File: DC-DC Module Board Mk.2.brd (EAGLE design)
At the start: 177.9 x 101.7 mm, 163 parts, among them Q1 FDN340P, U2 AP1117_LIN_REG, U3 LM1085IS-5.0

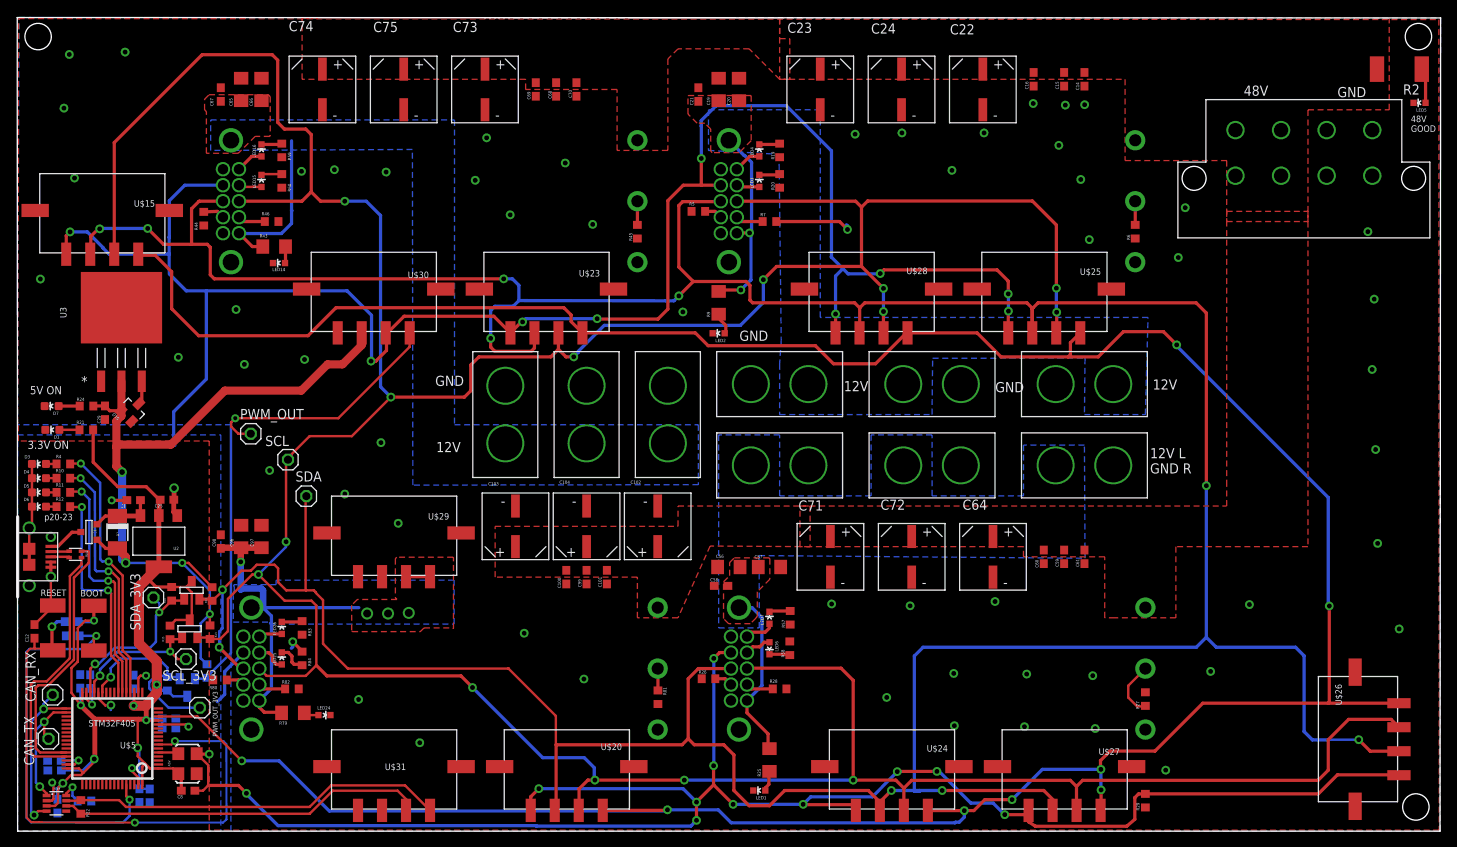
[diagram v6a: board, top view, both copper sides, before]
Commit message: cleaning up the trace
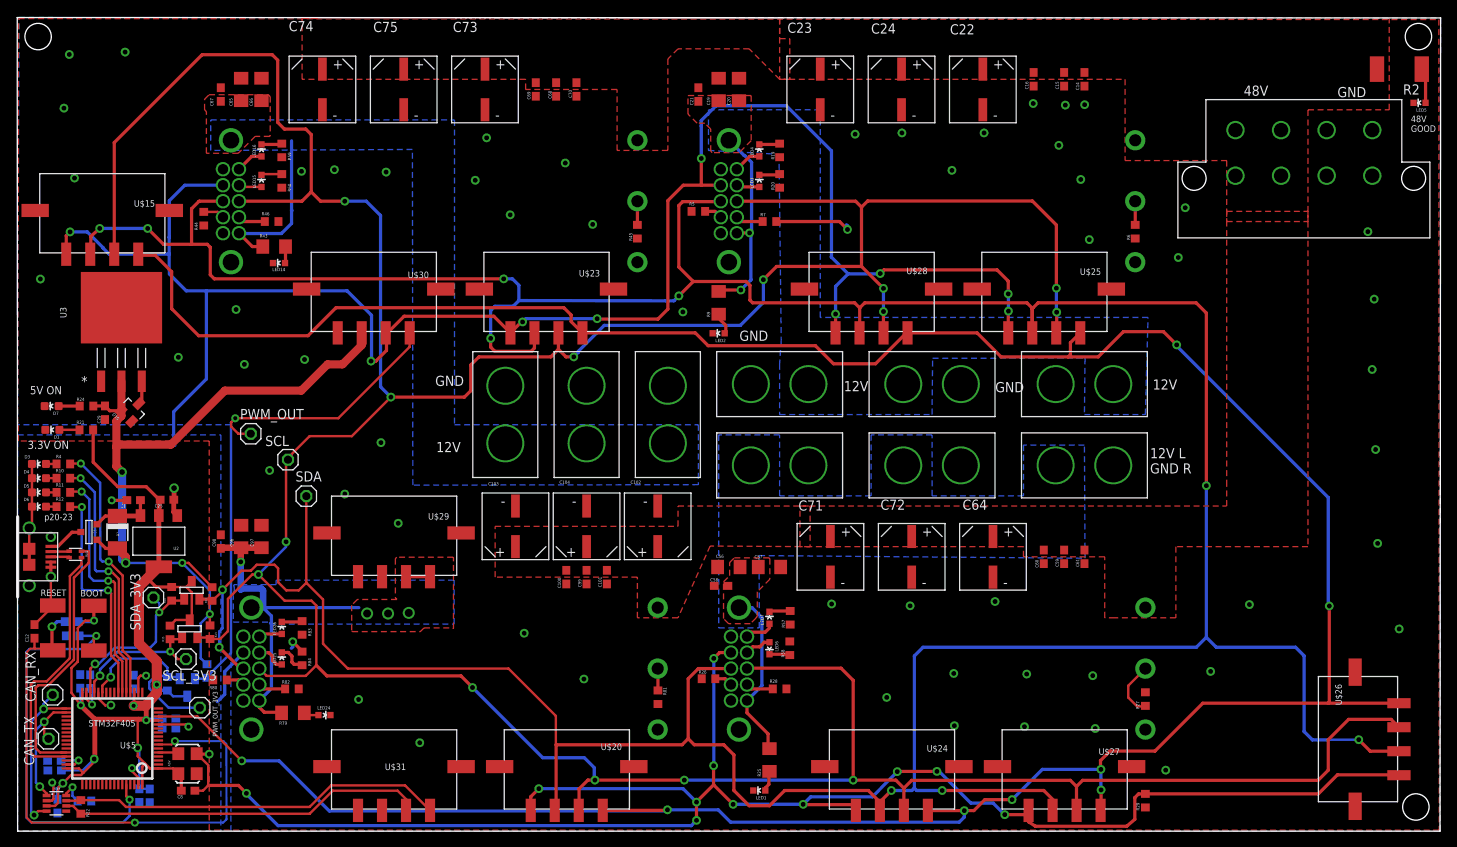
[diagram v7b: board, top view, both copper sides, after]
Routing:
- net SDA: track 516.2 -> 515.0 mm
- net DGND: track 504.1 -> 503.1 mm
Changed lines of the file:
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@@
 <wire x1="107.78" y1="2.37" x2="106.34" y2="3.81" width="0.4064" layer="1"/>
 <wire x1="106.34" y1="3.81" x2="95.885" y2="3.81" width="0.4064" layer="1"/>
-<wire x1="109.22" y1="3.81" x2="112.7252" y2="3.81" width="0.4064" layer="16"/>
-<wire x1="115.57" y1="3.81" x2="112.7252" y2="3.81" width="0.4064" layer="16"/>
 <wire x1="113.1824" y1="21.717" x2="147.3454" y2="21.717" width="0.4064" layer="16"/>
 <wire x1="147.3454" y1="21.717" x2="148.59" y2="22.9616" width="0.4064" layer="16"/>
@@
 <wire x1="81.026" y1="65.024" x2="82.042" y2="65.024" width="0.4064" layer="16"/>
 <wire x1="82.042" y1="65.024" x2="82.6516" y2="65.6336" width="0.4064" layer="16"/>
-<wire x1="112.0902" y1="20.6248" x2="112.0902" y2="3.7084" width="0.4064" layer="16"/>
-<wire x1="112.0902" y1="3.7084" x2="112.7252" y2="3.7084" width="0.4064" layer="16"/>
-<wire x1="112.7252" y1="3.7084" x2="112.7252" y2="3.81" width="0.4064" layer="16"/>
 <wire x1="22.7178" y1="27.729" x2="24.2022" y2="27.729" width="0.4064" layer="1"/>
 <wire x1="24.2022" y1="27.729" x2="24.3078" y2="27.5218" width="0.4064" layer="1"/>
@@
 <wire x1="18.2372" y1="72.0852" x2="16.256" y2="74.0664" width="0.4064" layer="1"/>
 <via x="16.256" y="74.0664" extent="1-16" drill="0.6"/>
-<wire x1="16.256" y1="74.0664" x2="10.3124" y2="74.0664" width="0.4064" layer="16"/>
-<wire x1="10.3124" y1="74.0664" x2="10.2616" y2="74.0156" width="0.4064" layer="16"/>
-<via x="10.2616" y="74.0156" extent="1-16" drill="0.6"/>
-<wire x1="10.2616" y1="74.0156" x2="10.0838" y2="74.0156" width="0.4064" layer="1"/>
-<wire x1="10.0838" y1="74.0156" x2="9.144" y2="73.0758" width="0.4064" layer="1"/>
+<via x="10.2616" y="74.0656" extent="1-16" drill="0.6"/>
 <wire x1="9.144" y1="73.0758" x2="9.144" y2="70.9132" width="0.4064" layer="1"/>
 <wire x1="9.144" y1="70.9132" x2="9.0756" y2="70.8448" width="0.4064" layer="1"/>
-<wire x1="33.5788" y1="28.829" x2="36.06" y2="28.829" width="0.3048" layer="1"/>
-<wire x1="36.06" y1="28.829" x2="37.0332" y2="28.829" width="0.3048" layer="1"/>
-<wire x1="37.0332" y1="28.829" x2="37.2872" y2="28.575" width="0.3048" layer="1"/>
-<wire x1="37.2872" y1="28.575" x2="37.2872" y2="28.4988" width="0.3048" layer="1"/>
-<wire x1="37.2872" y1="28.4988" x2="38.1762" y2="27.6098" width="0.3048" layer="1"/>
-<wire x1="38.1762" y1="27.6098" x2="38.1762" y2="22.1488" width="0.3048" layer="1"/>
+<wire x1="38.1762" y1="27.686" x2="38.1762" y2="22.1488" width="0.3048" layer="1"/>
 <wire x1="38.1762" y1="22.1488" x2="41.275" y2="19.05" width="0.3048" layer="1"/>
 <wire x1="29.1592" y1="31.2928" x2="29.8958" y2="32.0294" width="0.3048" layer="1"/>
@@
 <wire x1="67.277" y1="9.525" x2="67.277" y2="13.134" width="0.3048" layer="1"/>
 <contactref element="SDA" pad="1"/>
-<wire x1="61.361" y1="19.091" x2="61.361" y2="19.05" width="0.3048" layer="1"/>
-<wire x1="36" y1="40.52" x2="36" y2="28.889" width="0.3048" layer="1"/>
-<wire x1="36" y1="28.889" x2="36.06" y2="28.829" width="0.3048" layer="1"/>
-<wire x1="36" y1="40.52" x2="36.085" y2="40.605" width="0.3048" layer="1"/>
 <wire x1="28.21" y1="19.05" x2="27.8638" y2="19.05" width="0.4064" layer="1"/>
 <wire x1="27.8638" y1="19.05" x2="25.1968" y2="21.717" width="0.4064" layer="1"/>
+<wire x1="36.085" y1="29.7772" x2="38.1762" y2="27.686" width="0.3048" layer="1"/>
+<wire x1="36.085" y1="40.605" x2="36.085" y2="29.7772" width="0.3048" layer="1"/>
+<wire x1="36.085" y1="29.7772" x2="35.1368" y2="28.829" width="0.3048" layer="1"/>
+<wire x1="35.1368" y1="28.829" x2="33.5788" y2="28.829" width="0.3048" layer="1"/>
+<wire x1="16.256" y1="74.0664" x2="10.2616" y2="74.0656" width="0.4064" layer="16"/>
+<wire x1="9.144" y1="73.0758" x2="10.2616" y2="74.0656" width="0.4064" layer="1"/>
+<wire x1="112.0902" y1="20.6248" x2="112.0902" y2="4.1102" width="0.4064" layer="16"/>
+<wire x1="112.0902" y1="4.1102" x2="111.79" y2="3.81" width="0.4064" layer="16"/>
+<wire x1="111.79" y1="3.81" x2="109.22" y2="3.81" width="0.4064" layer="16"/>
+<wire x1="115.57" y1="3.81" x2="112.3904" y2="3.81" width="0.4064" layer="16"/>
+<wire x1="112.3904" y1="3.81" x2="112.0902" y2="4.1102" width="0.4064" layer="16"/>
 </signal>
 <signal name="ALERT">
@@
 <via x="98.1964" y="2.0828" extent="1-16" drill="0.6"/>
 <wire x1="104.5514" y1="2.0828" x2="104.78" y2="1.8542" width="0.4064" layer="1"/>
-<wire x1="64.8462" y1="-0.635" x2="84.1502" y2="-0.635" width="0.4064" layer="16"/>
-<wire x1="84.1502" y1="-0.635" x2="84.8614" y2="0.0762" width="0.4064" layer="16"/>
 <via x="84.8614" y="0.0762" extent="1-16" drill="0.6"/>
 <wire x1="84.8614" y1="0.0762" x2="84.8614" y2="2.353" width="0.4064" layer="1"/>
@@
 <wire x1="28.6004" y1="3.4544" x2="28.6004" y2="3.3782" width="0.4064" layer="16"/>
 <wire x1="28.6004" y1="3.3782" x2="32.5628" y2="-0.5842" width="0.4064" layer="16"/>
-<wire x1="32.5628" y1="-0.5842" x2="64.7954" y2="-0.5842" width="0.4064" layer="16"/>
-<wire x1="64.7954" y1="-0.5842" x2="64.8462" y2="-0.635" width="0.4064" layer="16"/>
 <wire x1="28.21" y1="21.05" x2="28.21" y2="20.9964" width="0.4064" layer="16"/>
 <wire x1="28.21" y1="20.9964" x2="25.8826" y2="18.669" width="0.4064" layer="16"/>
@@
 <contactref element="U$5" pad="28"/>
 <via x="11.6586" y="14.478" extent="1-16" drill="0.6"/>
-<wire x1="11.6586" y1="14.478" x2="11.6586" y2="13.8938" width="0.3048" layer="16"/>
-<wire x1="11.6586" y1="13.8938" x2="11.6332" y2="13.8684" width="0.3048" layer="16"/>
 <wire x1="6.0756" y1="70.8448" x2="6.0756" y2="73.157" width="0.4064" layer="1"/>
 <wire x1="6.0756" y1="73.157" x2="6.5532" y2="73.6346" width="0.4064" layer="1"/>
@@
 <wire x1="46.112" y1="60.913" x2="46.01" y2="61.015" width="0.4064" layer="1"/>
 <via x="102.24" y="63.368" extent="1-16" drill="0.6"/>
-<wire x1="102.24" y1="63.368" x2="102.24" y2="68.12" width="0.4064" layer="16"/>
 <wire x1="104.78" y1="2.037" x2="98.2422" y2="2.037" width="0.4064" layer="1"/>
 <wire x1="98.2422" y1="2.037" x2="98.1964" y2="2.0828" width="0.4064" layer="1"/>
@@
 <via x="84.8614" y="2.353" extent="1-16" drill="0.6"/>
 <wire x1="84.8614" y1="2.353" x2="84.8614" y2="2.3876" width="0.4064" layer="1"/>
-<wire x1="101.7" y1="70.5" x2="103.16" y2="69.04" width="0.4064" layer="16"/>
-<wire x1="103.16" y1="69.04" x2="103.81" y2="68.39" width="0.4064" layer="16"/>
+<wire x1="101.7" y1="70.5" x2="103.81" y2="68.39" width="0.4064" layer="16"/>
 <wire x1="103.81" y1="68.39" x2="107.7854" y2="68.39" width="0.4064" layer="16"/>
 <wire x1="107.7854" y1="68.39" x2="107.823" y2="68.4276" width="0.4064" layer="16"/>
-<wire x1="102.24" y1="68.12" x2="103.16" y2="69.04" width="0.4064" layer="16"/>
 <wire x1="20.9" y1="79.47" x2="18.96" y2="77.53" width="0.4064" layer="16"/>
 <wire x1="18.96" y1="77.53" x2="18.96" y2="72.992" width="0.4064" layer="16"/>
@@
 <wire x1="85.45" y1="86.89" x2="85.46" y2="86.88" width="0.4064" layer="16"/>
 <contactref element="C13" pad="2"/>
+<wire x1="102.24" y1="63.368" x2="102.24" y2="66.82" width="0.4064" layer="16"/>
+<wire x1="102.24" y1="66.82" x2="103.81" y2="68.39" width="0.4064" layer="16"/>
+<wire x1="84.8614" y1="0.0762" x2="84.201" y2="-0.5842" width="0.4064" layer="16"/>
+<wire x1="84.201" y1="-0.5842" x2="32.5628" y2="-0.5842" width="0.4064" layer="16"/>
 </signal>
 <signal name="VCAP_1">
@@
 <wire x1="25.6794" y1="-0.2032" x2="14.6558" y2="-0.2032" width="0.254" layer="16"/>
 <via x="14.6558" y="-0.2032" extent="1-16" drill="0.508"/>
-<wire x1="14.6558" y1="-0.2032" x2="1.7018" y2="-0.1524" width="0.254" layer="1"/>
-<wire x1="1.7018" y1="-0.1524" x2="1.1176" y2="0.4318" width="0.254" layer="1"/>
 <wire x1="1.1176" y1="0.4318" x2="1.1176" y2="21.082" width="0.254" layer="1"/>
 <wire x1="1.1176" y1="21.082" x2="1.5748" y2="21.5392" width="0.254" layer="1"/>
@@
 <wire x1="4.2926" y1="24.2824" x2="4.2926" y2="21.4316" width="0.4064" layer="1"/>
 <wire x1="4.2926" y1="21.4316" x2="4.3942" y2="21.33" width="0.4064" layer="1"/>
+<wire x1="14.6558" y1="-0.2032" x2="1.7526" y2="-0.2032" width="0.254" layer="1"/>
+<wire x1="1.7526" y1="-0.2032" x2="1.1176" y2="0.4318" width="0.254" layer="1"/>
 </signal>
 <signal name="BOOT0">
@@
 <via x="81.2292" y="1.397" extent="1-16" drill="0.6"/>
 <wire x1="81.2292" y1="1.397" x2="87.5792" y2="1.397" width="0.4064" layer="16"/>
-<wire x1="87.5792" y1="1.397" x2="89.2048" y2="-0.2286" width="0.4064" layer="16"/>
-<wire x1="89.2048" y1="-0.2286" x2="117.1702" y2="-0.2286" width="0.4064" layer="16"/>
-<wire x1="117.1702" y1="-0.2286" x2="117.2464" y2="-0.1524" width="0.4064" layer="16"/>
-<wire x1="117.2464" y1="-0.1524" x2="117.7036" y2="-0.1524" width="0.4064" layer="16"/>
 <wire x1="117.7036" y1="-0.1524" x2="118.3386" y2="0.4826" width="0.4064" layer="16"/>
 <wire x1="118.3386" y1="0.4826" x2="118.3386" y2="1.2954" width="0.4064" layer="16"/>
@@
 <wire x1="111.24" y1="60.8972" x2="110.986" y2="60.8972" width="0.4064" layer="1"/>
 <wire x1="110.986" y1="60.8972" x2="107.2388" y2="57.15" width="0.4064" layer="1"/>
+<wire x1="117.7036" y1="-0.1524" x2="89.1286" y2="-0.1524" width="0.4064" layer="16"/>
+<wire x1="89.1286" y1="-0.1524" x2="87.5792" y2="1.397" width="0.4064" layer="16"/>
 </signal>
 <signal name="PIN15">
@@
 <vertex x="83.7946" y="90.6526"/>
 </polygon>
-<wire x1="91.6686" y1="73.3298" x2="91.4908" y2="73.5076" width="0.4064" layer="1"/>
 <wire x1="91.6686" y1="67.6402" x2="91.6686" y2="73.3298" width="0.4064" layer="16"/>
 <wire x1="91.6686" y1="73.3298" x2="91.4908" y2="73.5076" width="0.4064" layer="16"/>
@@
 <contactref element="U$22" pad="9"/>
 <contactref element="R44" pad="2"/>
-<wire x1="23.2664" y1="76.1356" x2="24.94" y2="76.2" width="0.4064" layer="1"/>
-<wire x1="24.94" y1="76.2" x2="25.67" y2="75.47" width="0.4064" layer="1"/>
+<wire x1="23.2664" y1="76.1356" x2="25.0044" y2="76.1356" width="0.3048" layer="1"/>
+<wire x1="25.0044" y1="76.1356" x2="25.67" y2="75.47" width="0.3048" layer="1"/>
 </signal>
 <signal name="ADRS00A4">
